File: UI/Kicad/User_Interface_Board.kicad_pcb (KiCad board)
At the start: 2 copper layers, 71 x 62.8 mm, 13 parts, among them J1 BHR-16-HUA, J2 Conn_01x02_Male, J3 Conn_01x02_Male, J4 Conn_01x02_Male, J5 Conn_01x02_Male, J6 Conn_01x08_Male, J7 Conn_01x05_Male, J8 Conn_01x03_Male

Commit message: Display-Board Updated!
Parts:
- removed J7: Conn_01x05_Male, Connector_PinSocket_2.54mm:PinSocket_1x05_P2.54mm_Vertical
- removed J8: Conn_01x03_Male, Connector_PinHeader_2.54mm:PinHeader_1x03_P2.54mm_Vertical
- C1: value 1uF -> 1u; footprint Resistor_SMD:R_0805_2012Metric_Pad1.15x1.40mm_HandSolder -> Capacitor_SMD:C_0805_2012Metric
- J1: value BHR-16-HUA -> BHR-14-HUA; footprint User_Interface_Board:BHR-16-HUA -> User_Interface_Board:BHR-14-HUA
- J3: value Conn_01x02_Male -> Conn_01x03_Male; footprint Connector_PinHeader_2.54mm:PinHeader_1x02_P2.54mm_Vertical -> Connector_PinHeader_2.54mm:PinHeader_1x03_P2.54mm_Vertical
- J4: value Conn_01x02_Male -> Conn_01x08_Male; footprint Connector_PinHeader_2.54mm:PinHeader_1x02_P2.54mm_Vertical -> Connector_PinSocket_2.54mm:PinSocket_1x08_P2.54mm_Vertical
- J6: value Conn_01x08_Male -> Conn_01x05_Male; footprint Connector_PinSocket_2.54mm:PinSocket_1x08_P2.54mm_Vertical -> Connector_PinSocket_2.54mm:PinSocket_1x05_P2.54mm_Vertical
- R1, R3: value 10k -> 100k; footprint Resistor_SMD:R_0805_2012Metric_Pad1.15x1.40mm_HandSolder -> Resistor_SMD:R_0805_2012Metric; moved to F.Cu
- R2, R4: value 10k -> 220; footprint Resistor_SMD:R_0805_2012Metric_Pad1.15x1.40mm_HandSolder -> Resistor_SMD:R_0805_2012Metric; moved to F.Cu
- moved C1 65.1 mm to (89.8, 103.2), turned to 0 degrees
- moved J6 57.5 mm to (180.2, 117.4)
- moved R2 52.2 mm to (90.2, 111.3)
- moved R4 49.2 mm to (104.5, 111.2)
- moved J1 49.1 mm to (90.7, 88.1)
- moved J4 48.7 mm to (101.5, 77.2)
- moved J5 47.2 mm to (105.8, 118.5), turned to 180 degrees
- moved J3 46.9 mm to (101.1, 129.5), turned to 270 degrees
- moved J2 44.8 mm to (91.5, 118.5), turned to 180 degrees
- moved R1 44.3 mm to (92.8, 111.3), turned to 90 degrees
- moved R3 41.4 mm to (107.0, 111.3), turned to 90 degrees
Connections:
- C1 pad 1: /+3,3V -> /3,3V
- J1 pad 1: /Poti -> /3,3V
- J1 pad 10: /CLK -> /VRy
- J1 pad 11: /CS -> /VRx
- J1 pad 12: /DC -> /SW
- J1 pad 13: /RST -> /BACK_BUTTON
- J1 pad 14: /Busy -> /ENTER_BUTTON
- J1 pad 2: /Button4 -> GND
- J1 pad 3: /Button3 -> /DIN
- J1 pad 4: /Button2 -> /CLK
- J1 pad 5: /Button1 -> /CS
- J1 pad 6: GND -> /DC
- J1 pad 7: /SW -> /RST
- J1 pad 8: /X -> /BUSY
- J1 pad 9: /DIN -> /POTI
- J2 pad 1: /Button1 -> /3,3V
- J2 pad 2: GND -> Net-(J2-Pad2)
- J3 pad 1: /Button2 -> /3,3V
- J3 pad 2: GND -> /POTI
- J4 pad 1: /Button3 -> /3,3V
- J5 pad 1: /Button4 -> /3,3V
- J5 pad 2: GND -> Net-(J5-Pad2)
- J6 pad 1: /Busy -> /SW
- J6 pad 2: /RST -> /VRy
- J6 pad 3: /DC -> /VRx
- J6 pad 4: /CS -> /3,3V
- J6 pad 5: /CLK -> GND
- R1 pad 1: /+3,3V -> Net-(J2-Pad2)
- R1 pad 2: /Button1 -> GND
- R2 pad 1: /+3,3V -> /BACK_BUTTON
- R2 pad 2: /Button2 -> Net-(J2-Pad2)
- R3 pad 1: /+3,3V -> Net-(J5-Pad2)
- R3 pad 2: /Button3 -> GND
- R4 pad 1: /+3,3V -> /ENTER_BUTTON
- R4 pad 2: /Button4 -> Net-(J5-Pad2)
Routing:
- net /3,3V: track 0.00 -> 166.9 mm, vias 0 -> 1
- net /+3,3V: track 120.7 -> 0.00 mm, vias 6 -> 0
- net /VRx: track 0.00 -> 104.6 mm
- net /VRy: track 0.00 -> 99.7 mm
- net /X: track 82.5 -> 0.00 mm
- net /Y: track 80.0 -> 0.00 mm
- net GND: track 70.5 -> 0.00 mm
- net /Poti: track 49.2 -> 0.00 mm
- net /POTI: track 0.00 -> 43.7 mm
- net /RST: track 7.64 -> 47.7 mm
- net /Button4: track 30.5 -> 0.00 mm
- net /Button3: track 29.2 -> 0.00 mm
- net /Button1: track 28.7 -> 0.00 mm
- net /CS: track 7.64 -> 36.0 mm
- net /Button2: track 27.9 -> 0.00 mm
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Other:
- board size 71 x 62.8 mm -> 101 x 65 mm
- board text added: "3,3V"
- board text added: "BUSY"
- board text added: "CLK"
- board text added: "CS"
- board text added: "DC"
- board text added: "DIN"
- board text added: "DSP-Projekt SS 2021 GUI-Board"
- board text added: "GND"
- board text added: "Joystick KY-023"
- board text added: "Poti"
- board text added: "RST"
- board text added: "SW"
- board text added: "VRx"
- board text added: "VRy"
- board text added: "Waveshare 1.54inch e-Paper Display"
- board text removed: "1"
- board text removed: "3V3 Poti GND"
- board text removed: "3V3 SW X Y GND"
- board text removed: "Busy RST DC CS CLK DIN GND 3V3"
- board text removed: "DSP LAB WS19/20 User Interface"
- board text removed: "Waveshare 1.54inch E-Ink display module"

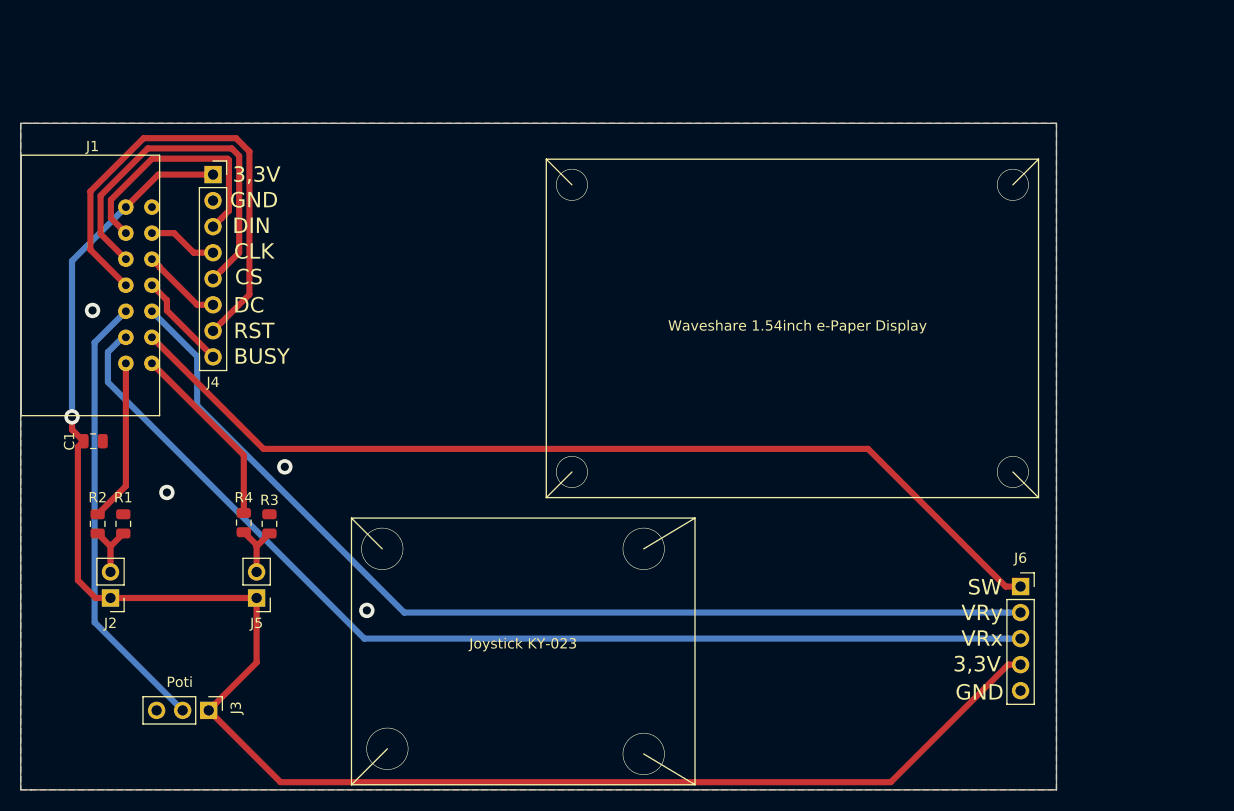
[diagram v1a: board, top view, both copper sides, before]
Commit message: changed orientation of the display
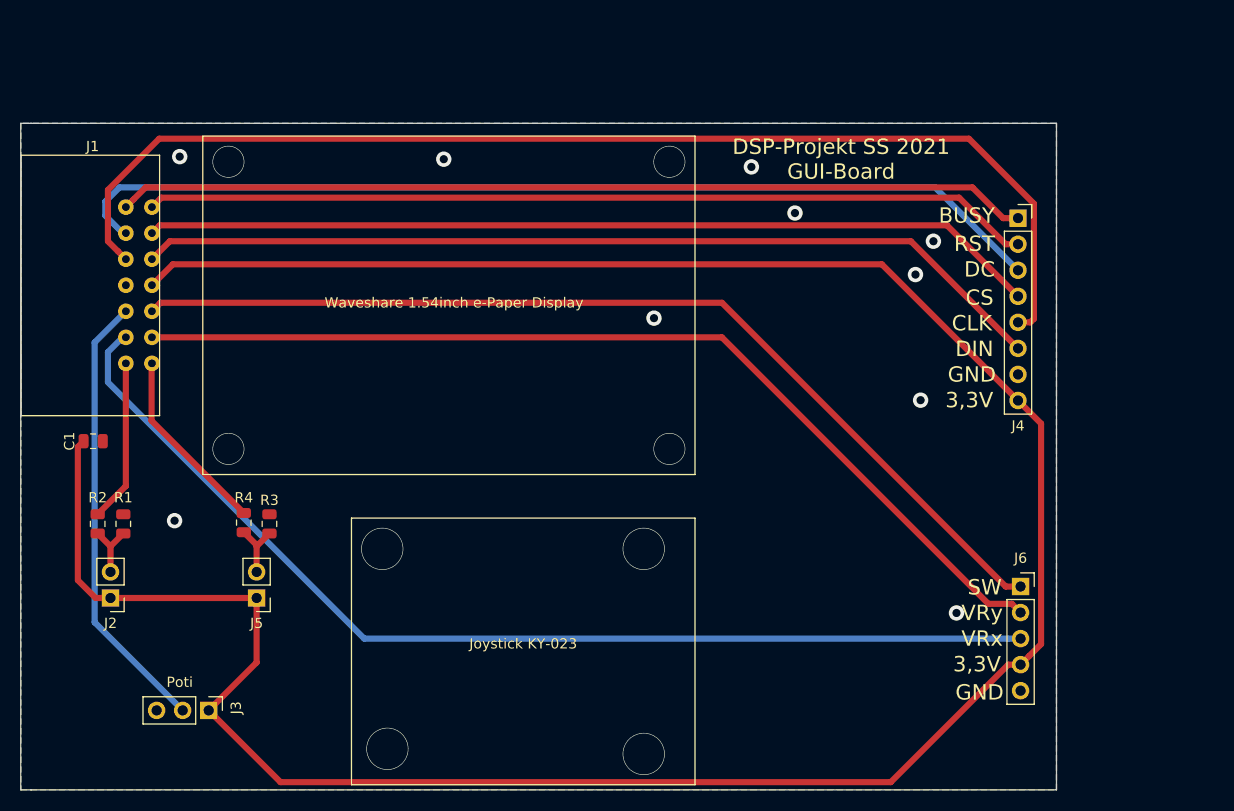
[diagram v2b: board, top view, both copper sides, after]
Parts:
- moved J4 78.6 mm to (180.0, 81.5)
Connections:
- J1 pad 1: /3,3V -> /BUSY
- J1 pad 10: /VRy -> /SW
- J1 pad 12: /SW -> /VRy
- J1 pad 2: GND -> /RST
- J1 pad 3: /DIN -> /DC
- J1 pad 4: /CLK -> /CS
- J1 pad 5: /CS -> /CLK
- J1 pad 6: /DC -> /DIN
- J1 pad 7: /RST -> GND
- J1 pad 8: /BUSY -> /3,3V
- J4 pad 1: /3,3V -> /BUSY
- J4 pad 2: GND -> /RST
- J4 pad 3: /DIN -> /DC
- J4 pad 4: /CLK -> /CS
- J4 pad 5: /CS -> /CLK
- J4 pad 6: /DC -> /DIN
- J4 pad 7: /RST -> GND
- J4 pad 8: /BUSY -> /3,3V
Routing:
- net /CLK: track 6.75 -> 115.4 mm
- net /DC: track 7.83 -> 97.0 mm
- net /3,3V: track 166.9 -> 250.0 mm, vias 1 -> 0
- net /BUSY: track 9.46 -> 89.0 mm
- net /DIN: track 24.2 -> 89.5 mm
- net /CS: track 36.0 -> 87.6 mm
- net /RST: track 47.7 -> 86.7 mm
- net /VRy: track 99.7 -> 95.8 mm
- net /SW: track 94.8 -> 96.5 mm
- net GND: vias 4 -> 10

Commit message: Bemaßung hinzugefügt
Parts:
- moved J3 4.75 mm to (101.1, 134.2)
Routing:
- net /POTI: track 43.7 -> 48.5 mm
- net /3,3V: track 250.0 -> 252.2 mm
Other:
- board text added: "Btn1"
- board text added: "Btn2"
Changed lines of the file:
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@@
   (general
     (thickness 1.6)
-    (drawings 48)
-    (tracks 96)
+    (drawings 62)
+    (tracks 98)
     (zones 0)
     (modules 11)
@@
   )
   (module Connector_PinHeader_2.54mm:PinHeader_1x03_P2.54mm_Vertical (layer F.Cu)
-    (at 101.08 129.5 270)
+    (at 101.08 134.25 270)
     (descr "Through hole straight pin header, 1x03, 2.54mm pitch, single row")
     (tags "Through hole pin header THT 1x03 2.54mm single row")
-    (fp_text reference J3 (at -0.25 -2.67 90) (layer F.SilkS)
-      (effects (font (size 1 1) (thickness 0.15)))
-    )
-    (fp_text value Conn_01x03_Male (at 0 7.41 90) (layer F.Fab)
+    (fp_text reference J3 (at 0 7.33 90) (layer F.SilkS)
+      (effects (font (size 1 1) (thickness 0.15)))
+    )
+    (fp_text value Conn_01x03_Male (at -2.5 2.83 180) (layer F.Fab)
       (effects (font (size 1 1) (thickness 0.15)))
     )
@@
       (effects (font (size 1 1) (thickness 0.15)))
     )
-    (fp_text value Conn_01x05_Male (at -3.5 13.83) (layer F.Fab)
+    (fp_text value Conn_01x05_Male (at -4 13.83) (layer F.Fab)
       (effects (font (size 1 1) (thickness 0.15)))
     )
@@
     )
   )
+  (dimension 36.490022 (width 0.15) (layer Eco2.User)
+    (gr_text "36,490 mm" (at 79.280377 119.001175 89.93719292) (layer Eco2.User)
+      (effects (font (size 1 1) (thickness 0.15)))
+    )
+    (feature1 (pts (xy 82.79 100.76) (xy 80.013956 100.756957)))
+    (feature2 (pts (xy 82.75 137.25) (xy 79.973956 137.246957)))
+    (crossbar (pts (xy 80.560376 137.2476) (xy 80.600376 100.7576)))
+    (arrow1a (pts (xy 80.600376 100.7576) (xy 81.185562 101.884746)))
+    (arrow1b (pts (xy 80.600376 100.7576) (xy 80.012721 101.88346)))
+    (arrow2a (pts (xy 80.560376 137.2476) (xy 81.148031 136.12174)))
+    (arrow2b (pts (xy 80.560376 137.2476) (xy 79.97519 136.120454)))
+  )
+  (dimension 3.1 (width 0.15) (layer Eco2.User)
+    (gr_text "3,100 mm" (at 79.35 73.8 270) (layer Eco2.User)
+      (effects (font (size 1 1) (thickness 0.15)))
+    )
+    (feature1 (pts (xy 82.75 75.35) (xy 80.063579 75.35)))
+    (feature2 (pts (xy 82.75 72.25) (xy 80.063579 72.25)))
+    (crossbar (pts (xy 80.65 72.25) (xy 80.65 75.35)))
+    (arrow1a (pts (xy 80.65 75.35) (xy 80.063579 74.223496)))
+    (arrow1b (pts (xy 80.65 75.35) (xy 81.236421 74.223496)))
+    (arrow2a (pts (xy 80.65 72.25) (xy 80.063579 73.376504)))
+    (arrow2b (pts (xy 80.65 72.25) (xy 81.236421 73.376504)))
+  )
+  (gr_line (start 102 126.75) (end 95 126.75) (layer Eco2.User) (width 0.15))
+  (gr_line (start 98.5 123.25) (end 98.5 130.25) (layer Eco2.User) (width 0.15))
+  (gr_line (start 105.75 117.25) (end 100.25 117.25) (layer Eco2.User) (width 0.15))
+  (gr_line (start 105.75 117.25) (end 111.25 117.25) (layer Eco2.User) (width 0.15))
+  (gr_line (start 105.75 117.25) (end 105.75 122.75) (layer Eco2.User) (width 0.15))
+  (gr_line (start 105.75 117.25) (end 105.7 111.8) (layer Eco2.User) (width 0.15))
+  (gr_line (start 91.5 117.25) (end 91.5 122.75) (layer Eco2.User) (width 0.15))
+  (gr_line (start 91.5 117.3) (end 91.5 111.75) (layer Eco2.User) (width 0.15))
+  (gr_line (start 91.5 117.3) (end 86 117.3) (layer Eco2.User) (width 0.15))
+  (gr_line (start 91.5 117.3) (end 97 117.3) (layer Eco2.User) (width 0.15))
+  (gr_line (start 148.5 110.75) (end 143.5 113.75) (layer Eco2.User) (width 0.15))
+  (gr_line (start 148.5 136.75) (end 143.5 133.75) (layer Eco2.User) (width 0.15))
+  (gr_line (start 115 110.75) (end 118 113.75) (layer Eco2.User) (width 0.15))
+  (gr_line (start 115 136.75) (end 118 133.75) (layer Eco2.User) (width 0.15))
+  (target plus (at 82.75 137.25) (size 5) (width 0.05) (layer Edge.Cuts))
+  (gr_text Btn2 (at 99.25 115.25 90) (layer F.SilkS)
+    (effects (font (size 1 1) (thickness 0.15)))
+  )
+  (gr_text Btn1 (at 85.25 117.25 90) (layer F.SilkS)
+    (effects (font (size 1 1) (thickness 0.15)))
+  )
   (dimension 65 (width 0.15) (layer Eco2.User)
     (gr_text "65,000 mm" (at 69.2 104.75 90) (layer Eco2.User)
@@
     (effects (font (size 1.5 1.5) (thickness 0.3)))
   )
-  (target plus (at 82.75 137.25) (size 5) (width 0.05) (layer Edge.Cuts))
   (gr_line (start 82.75 72.25) (end 83.75 72.25) (layer Edge.Cuts) (width 0.05))
   (gr_line (start 82.75 100.75) (end 82.75 72.25) (layer Edge.Cuts) (width 0.05))
@@
   (gr_circle (center 91.5 117.25) (end 97 117.25) (layer Eco2.User) (width 0.05))
   (gr_circle (center 105.75 117.25) (end 111.25 117.25) (layer Eco2.User) (width 0.05))
-  (gr_circle (center 98.5 129.5) (end 103 129.5) (layer Eco2.User) (width 0.05))
+  (gr_circle (center 98.5 126.75) (end 102 126.75) (layer Eco2.User) (width 0.05))
   (gr_text Poti (at 98.25 126.75) (layer F.SilkS)
     (effects (font (size 1 1) (thickness 0.15)))
   )
-  (gr_text "Joystick KY-023" (at 131.75 123) (layer F.SilkS)
+  (gr_text "Joystick KY-023" (at 131.75 124.25) (layer F.SilkS)
     (effects (font (size 1 1) (thickness 0.15)))
   )
-  (gr_line (start 148.5 110.75) (end 143.5 113.75) (layer Eco2.User) (width 0.12))
-  (gr_line (start 148.5 136.75) (end 143.5 133.75) (layer Eco2.User) (width 0.12))
-  (gr_line (start 115 136.75) (end 118.5 133.25) (layer Eco2.User) (width 0.12))
-  (gr_line (start 115 110.75) (end 118 113.75) (layer Eco2.User) (width 0.12))
   (gr_line (start 115 136.75) (end 115 110.75) (layer F.SilkS) (width 0.12))
   (gr_line (start 148.5 136.75) (end 115 136.75) (layer F.SilkS) (width 0.12))
@@
   (gr_line (start 148.5 73.5) (end 146 76) (layer Eco2.User) (width 0.12))
   (gr_line (start 100.5 73.5) (end 103 76) (layer Eco2.User) (width 0.12))
-  (gr_text "Waveshare 1.54inch e-Paper Display" (at 125 89.75) (layer F.SilkS)
+  (gr_text "Waveshare 1.54inch e-Paper Display" (at 124.25 95.25) (layer F.SilkS)
     (effects (font (size 1 1) (thickness 0.15)))
   )
@@
   (via (at 146 104) (size 3.1) (drill 3) (layers F.Cu B.Cu) (net 0))
   (via (at 143.5 133.75) (size 4.1) (drill 4) (layers F.Cu B.Cu) (net 0))
+  (via (at 118 113.75) (size 4.1) (drill 4) (layers F.Cu B.Cu) (net 0))
+  (via (at 118 133.75) (size 4.1) (drill 4) (layers F.Cu B.Cu) (net 0))
   (via (at 143.5 113.75) (size 4.1) (drill 4) (layers F.Cu B.Cu) (net 0))
-  (via (at 118 113.75) (size 4.1) (drill 4) (layers F.Cu B.Cu) (net 0))
-  (via (at 118.5 133.25) (size 4.1) (drill 4) (layers F.Cu B.Cu) (net 0))
   (segment (start 96.37 89.75) (end 95.54 90.58) (width 0.6) (layer F.Cu) (net 1))
   (segment (start 151.13 89.75) (end 96.37 89.75) (width 0.6) (layer F.Cu) (net 1))
@@
   (segment (start 104.3 118.54) (end 91.5 118.54) (width 0.6) (layer F.Cu) (net 8))
   (segment (start 105.75 118.54) (end 104.3 118.54) (width 0.6) (layer F.Cu) (net 8))
-  (segment (start 105.75 124.83) (end 101.08 129.5) (width 0.6) (layer F.Cu) (net 8))
   (segment (start 105.75 118.54) (end 105.75 124.83) (width 0.6) (layer F.Cu) (net 8))
-  (segment (start 108.080001 136.500001) (end 101.08 129.5) (width 0.6) (layer F.Cu) (net 8))
-  (segment (start 167.587918 136.500001) (end 108.080001 136.500001) (width 0.6) (layer F.Cu) (net 8))
-  (segment (start 180.25 125.04) (end 179.047919 125.04) (width 0.6) (layer F.Cu) (net 8))
   (segment (start 97.58 86) (end 95.54 88.04) (width 0.6) (layer F.Cu) (net 8))
   (segment (start 180 99.28) (end 166.72 86) (width 0.6) (layer F.Cu) (net 8))
   (segment (start 166.72 86) (end 97.58 86) (width 0.6) (layer F.Cu) (net 8))
-  (segment (start 179.047919 125.04) (end 167.587918 136.500001) (width 0.6) (layer F.Cu) (net 8))
   (segment (start 181.099999 124.190001) (end 180.25 125.04) (width 0.6) (layer F.Cu) (net 8))
   (segment (start 182.25 123.04) (end 181.099999 124.190001) (width 0.6) (layer F.Cu) (net 8))
   (segment (start 180 99.28) (end 182.25 101.53) (width 0.6) (layer F.Cu) (net 8))
   (segment (start 182.25 101.53) (end 182.25 123.04) (width 0.6) (layer F.Cu) (net 8))
+  (segment (start 105.75 131.03) (end 105.75 124.83) (width 0.6) (layer F.Cu) (net 8))
+  (segment (start 102.53 134.25) (end 105.75 131.03) (width 0.6) (layer F.Cu) (net 8))
+  (segment (start 101.08 134.25) (end 102.53 134.25) (width 0.6) (layer F.Cu) (net 8))
+  (segment (start 104.780001 136.500001) (end 102.53 134.25) (width 0.6) (layer F.Cu) (net 8))
+  (segment (start 167.587918 136.500001) (end 104.780001 136.500001) (width 0.6) (layer F.Cu) (net 8))
+  (segment (start 180.25 125.04) (end 179.047919 125.04) (width 0.6) (layer F.Cu) (net 8))
+  (segment (start 179.047919 125.04) (end 167.587918 136.500001) (width 0.6) (layer F.Cu) (net 8))
   (segment (start 95.5 101.25) (end 104.5 110.25) (width 0.6) (layer F.Cu) (net 9))
   (segment (start 95.54 95.66) (end 95.5 95.7) (width 0.6) (layer F.Cu) (net 9))
@@
   (segment (start 90.25 110.375) (end 93 107.625) (width 0.6) (layer F.Cu) (net 11))
   (segment (start 93 107.625) (end 93 95.66) (width 0.6) (layer F.Cu) (net 11))
-  (segment (start 89.949999 120.909999) (end 98.54 129.5) (width 0.6) (layer B.Cu) (net 12))
-  (segment (start 89.949999 93.630001) (end 89.949999 120.909999) (width 0.6) (layer B.Cu) (net 12))
+  (segment (start 89.949999 125.659999) (end 98.54 134.25) (width 0.6) (layer B.Cu) (net 12))
   (segment (start 93 90.58) (end 89.949999 93.630001) (width 0.6) (layer B.Cu) (net 12))
+  (segment (start 89.949999 93.630001) (end 89.949999 125.659999) (width 0.6) (layer B.Cu) (net 12))
   (segment (start 179.400001 119.110001) (end 177.110001 119.110001) (width 0.6) (layer F.Cu) (net 13))
   (segment (start 180.25 119.96) (end 179.400001 119.110001) (width 0.6) (layer F.Cu) (net 13))
